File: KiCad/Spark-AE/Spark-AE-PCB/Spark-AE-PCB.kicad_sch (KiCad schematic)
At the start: 16 parts, among them J1 SSM-120-L-SV-BE, J2 SSM-120-L-SV-BE, J3 Conn_02x10_Odd_Even, J4 Conn_02x05_Odd_Even, J5 Conn_01x08_Socket, J6 Conn_01x08_Socket, J7 UJ32-C-V-G-TH-5-P24-TR, SW1 SW_Push, SW2 SW_Push, U1 PJS008U-3000-0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

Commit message: moving over progress from "Shock" (see desc)
I attempted to create this Daisy Pod clone as an AE-1U module called the "Shock". As expected I couldn't make it work.

I've moved my progress on the "Shock" schematic over to and replacing the work on the "Spark".

I plan to go back to make the "Shock" a stripped down version of the "Spark" in an AE-1U format.
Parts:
- removed J1, J2: SSM-120-L-SV-BE, clectric-diy:SAMTEC_SSM-120-L-SV-BE, symbol clectric-diy:SSM-120-L-SV-BE
- removed J3: Conn_02x10_Odd_Even, Connector_PinHeader_2.54mm:PinHeader_2x10_P2.54mm_Vertical, symbol Connector_Generic:Conn_02x10_Odd_Even
- removed J5, J6: Conn_01x08_Socket, Connector_PinSocket_2.54mm:PinSocket_1x08_P2.54mm_Vertical, symbol Connector:Conn_01x08_Socket
- removed J7: UJ32-C-V-G-TH-5-P24-TR, clectric-diy:SAMESKY_UJ32-C-V-G-TH-5-P24-TR, symbol clectric-diy:UJ32-C-V-G-TH-5-P24-TR
- removed LED1, LED2: WS2812B-V5/W, clectric-diy:LED-SMD_4P-L5.0-W5.0-TL-1, symbol clectric-diy:WS2812B-V5_W
- removed R1, R2: RK09K1130A8G, clectric-diy:RES-TH_RK09K113004U, symbol clectric-diy:RK09K1130A8G
- removed U1: PJS008U-3000-0, clectric-diy:PJS008U-3000-0, symbol clectric-diy:PJS008U-3000-0
- removed U2: Daisy_Seed, clectric-diy:DAISY_SEED, symbol clectric-diy:Daisy_Seed
- added C1, C2, C3: 10nF, Capacitor_SMD:C_0402_1005Metric, symbol Device:C
- added D1, D10, D11, D12, D13, D14, D15, D16, D17, D18, D2, D3, D4, D5, D6, D7, D8, D9: D, Diode_SMD:D_0402_1005Metric, symbol Device:D
- added J1, J2: Conn_01x09_Socket, Connector_PinSocket_2.54mm:PinSocket_1x09_P2.54mm_Vertical, symbol Connector:Conn_01x09_Socket
- added J3, J4: Conn_01x20_Pin, clectric-diy:Connector_PinSocket-1x20-P2.54mm_Mill-Max_315-13-120-41-004000, symbol Connector:Conn_01x20_Pin
- added J6: Conn_02x05_Odd_Even, Connector_PinHeader_2.54mm:PinHeader_2x05_P2.54mm_Vertical, symbol Connector_Generic:Conn_02x05_Odd_Even
- added LED1, LED2: A-SP1943B1GHR6C-C01-2T, clectric-diy:LED-SMD_4P-L1.6-W1.5-BL_A-SP1943B1GHR6C-C01-2T, symbol clectric-diy:LED-SMD_4P-L1.6-W1.5-BL_A-SP1943B1GHR6C-C01-2T
- added NT1: NetTie, NetTie:NetTie-3_SMD_Pad0.5mm, symbol Device:NetTie_3
- added POT1, POT2: RK09K1130D62, clectric-diy:RK09K1130D62, symbol clectric-diy:RK09K1130A8G
- added R1, R2, R4, R5: 150R, Resistor_SMD:R_0402_1005Metric, symbol clectric-diy:CR0603-FX-1001ELF
- added R10, R11, R12, R7, R8, R9: 10K, Resistor_SMD:R_0402_1005Metric, symbol Device:R
- added R3, R6: 330R, Resistor_SMD:R_0402_1005Metric, symbol clectric-diy:CR0603-FX-1001ELF
- added U1: WS2811, clectric-diy:SOP-8_L4.9-W3.9-P1.27-LS6.0-BL, symbol clectric-diy:WS2811
- added U3: Daisy_Seed, clectric-diy:DAISY_SEED, symbol clectric-diy:Daisy_Seed
- renumbered S1 to ENC1, J4 to J5
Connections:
- net +3V3_A: now also J3.1 (Pin_1), J6.1 (Pin_1), POT1.3, POT2.3, U3.21 (3V3_A)
- net +3V3_D: now also J3.18 (Pin_18), J6.2 (Pin_2), LED1.3, LED2.3, R10.2, R11.2, R9.2, U3.38 (3V3_D)
- net +5V: now also ENC1.5 (+_2), J3.19 (Pin_19), U1.8 (VDD), U3.39 (VIN)
- net A1_D16: now also D17.2 (A), D8.1 (K), J3.3 (Pin_3), U3.23 (D16)
- net A7_D22: now also D18.2 (A), D9.1 (K), J3.9 (Pin_9), U3.29 (D22)
- net AUDIO_IN_1: now also D1.1 (K), J4.16 (Pin_16), U3.16 (AUDIO_IN_1)
- net AUDIO_IN_2: now also D2.1 (K), J4.17 (Pin_17), U3.17 (AUDIO_IN_2)
- net AUDIO_OUT_1: now also D10.2 (A), J4.18 (Pin_18), U3.18 (AUDIO_OUT_1)
- net AUDIO_OUT_2: now also D11.2 (A), J4.19 (Pin_19), U3.19 (AUDIO_OUT_2)
- net ENC_A: now also J3.13 (Pin_13), R7.2, U3.33 (D26)
- net ENC_B: now also J3.12 (Pin_12), R8.2, U3.32 (D25)
- net ENC_CLICK: now also J4.14 (Pin_14), R12.2, U3.14 (D13)
- net GND: now also NT1.3
- net I2C_SCL: now also J4.12 (Pin_12), J6.5 (Pin_5), U3.12 (D11)
- net I2C_SDA: now also J4.13 (Pin_13), J6.6 (Pin_6), U3.13 (D12)
- net LED_1_B: now also J3.5 (Pin_5), LED1.2, R2.1, R2.2, U3.25 (D18)
- net LED_1_G: now also J3.6 (Pin_6), LED1.1, R1.1, R1.2, U3.26 (D19)
- net LED_1_R: now also J3.7 (Pin_7), LED1.4, R3.1, R3.2, U3.27 (D20)
- net LED_2_B: now also J3.10 (Pin_10), LED2.2, R5.1, R5.2, U3.30 (D23)
- net LED_2_G: now also J3.11 (Pin_11), LED2.1, R4.1, R4.2, U3.31 (D24)
- net LED_2_R: now also J3.4 (Pin_4), LED2.4, R6.1, R6.2, U3.24 (D17)
- net POT_1: now also J3.8 (Pin_8), POT1.2, U3.28 (D21)
- net POT_2: now also J3.2 (Pin_2), POT2.2, U3.22 (D15)
- net SD_CK: now also J4.7 (Pin_7), U3.7 (D6)
- net SD_CMD: now also J4.6 (Pin_6), U3.6 (D5)
- net SD_D0: now also J4.5 (Pin_5), U3.5 (D4)
- net SD_D1: now also J4.4 (Pin_4), U3.4 (D3)
- net SD_D2: now also J4.3 (Pin_3), U3.3 (D2)
- net SD_D3: now also J4.2 (Pin_2), U3.2 (D1)
- net SPI_MISO: now also J4.10 (Pin_10), J6.10 (Pin_10), U3.10 (D9)
- net SPI_MOSI: now also J4.11 (Pin_11), J6.8 (Pin_8), U1.6 (DIN), U3.11 (D10)
- net SPI_NSS: now also J4.8 (Pin_8), J6.7 (Pin_7), U3.8 (D7)
- net SPI_SCK: now also J4.9 (Pin_9), J6.9 (Pin_9), U3.9 (D8)
- net TAC_SWITCH_1: now also SW1.1, J3.14 (Pin_14), U3.34 (D27)
- net TAC_SWITCH_2: now also SW2.1, J3.15 (Pin_15), U3.35 (D28)
- net USB_OTG_FS_D+: now also J3.17 (Pin_17), U3.37 (D30)
- net USB_OTG_FS_D-: now also J3.16 (Pin_16), U3.36 (D29)
- net USB_OTG_FS_ID: now also J4.1 (Pin_1), U3.1 (D0)
- net AGND: now reaches SW2.2
- net AGND: now also SW1.2, J4.20 (Pin_20), J6.3 (Pin_3), NT1.2, POT1.1, POT1.4 (EH), POT1.5 (EH), POT2.1, POT2.4 (EH), POT2.5 (EH), U3.20 (AGND)
- net ENC_RED: now reaches ENC1.1 (-_1)
- net ENC_RED: now also U1.1 (OUTR)
- net ENC_GREEN: now reaches ENC1.2 (-_2)
- net ENC_GREEN: now also U1.2 (OUTG)
- net at ENC1.3 (COM): now also C3.1, R11.1, R12.1
- net ENC_BLUE: now reaches ENC1.4 (+_1)
- net ENC_BLUE: now also U1.3 (OUTB)
- net at ENC1.A1: now also C1.1, R7.1, R9.1
- net at ENC1.B1: now also C2.1, R10.1, R8.1
- net DGND: now reaches ENC1.C1
- net DGND: now also ENC1.MH1, ENC1.MH2, C1.2, C2.2, C3.2, J3.20 (Pin_20), J6.4 (Pin_4), NT1.1, U1.4 (GND), U3.40 (DGND)
- new net D14: D16.2 (A), D7.1 (K), J4.15 (Pin_15), U3.15 (D14)
- new net POT1_CV: D5.1 (K)
- new net POT2_CV: D6.1 (K)
- new net SW1_CV: D3.1 (K)
- new net SW2_CV: D4.1 (K)
- no-connect marks 0 -> 6
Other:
- title: Spark-AE-Upper -> Spark-AE-PCB
- moved on the sheet: ENC1, J5, SW1, SW2

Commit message: initial committ of completely reworked schematic. thanks gemini!
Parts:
- removed C1, C2, C3: 10nF, Capacitor_SMD:C_0402_1005Metric, symbol Device:C
- removed D1, D10, D11, D12, D13, D14, D15, D16, D17, D18, D2, D3, D4, D5, D6, D7, D8, D9: D, Diode_SMD:D_0402_1005Metric, symbol Device:D
- removed ENC1: PEL12T-4225S-S1024, clectric-diy:PEL12T4225SS1024, symbol clectric-diy:PEL12T-4225S-S1024
- removed J1, J2: Conn_01x09_Socket, Connector_PinSocket_2.54mm:PinSocket_1x09_P2.54mm_Vertical, symbol Connector:Conn_01x09_Socket
- removed J3, J4: Conn_01x20_Pin, clectric-diy:Connector_PinSocket-1x20-P2.54mm_Mill-Max_315-13-120-41-004000, symbol Connector:Conn_01x20_Pin
- removed J5, J6: Conn_02x05_Odd_Even, Connector_PinHeader_2.54mm:PinHeader_2x05_P2.54mm_Vertical, symbol Connector_Generic:Conn_02x05_Odd_Even
- removed LED1, LED2: A-SP1943B1GHR6C-C01-2T, clectric-diy:LED-SMD_4P-L1.6-W1.5-BL_A-SP1943B1GHR6C-C01-2T, symbol clectric-diy:LED-SMD_4P-L1.6-W1.5-BL_A-SP1943B1GHR6C-C01-2T
- removed NT1: NetTie, NetTie:NetTie-3_SMD_Pad0.5mm, symbol Device:NetTie_3
- removed POT1, POT2: RK09K1130D62, clectric-diy:RK09K1130D62, symbol clectric-diy:RK09K1130A8G
- removed R1, R2, R4, R5: 150R, Resistor_SMD:R_0402_1005Metric, symbol clectric-diy:CR0603-FX-1001ELF
- removed R10, R11, R12, R7, R8, R9: 10K, Resistor_SMD:R_0402_1005Metric, symbol Device:R
- removed R3, R6: 330R, Resistor_SMD:R_0402_1005Metric, symbol clectric-diy:CR0603-FX-1001ELF
- removed SW1, SW2: SW_Push, Button_Switch_THT:SW_PUSH_6mm, symbol Switch:SW_Push
- removed U1: WS2811, clectric-diy:SOP-8_L4.9-W3.9-P1.27-LS6.0-BL, symbol clectric-diy:WS2811
- removed U3: Daisy_Seed, clectric-diy:DAISY_SEED, symbol clectric-diy:Daisy_Seed
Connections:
- no-connect marks 6 -> 0
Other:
- added sheet Daisy Seed & Mount (Spark-AE-PCB-DaisySeed.kicad_sch)
- added sheet Digital Expansion (Spark-AE-PCB-Expansion.kicad_sch)
- added sheet Input & Output (1 of 2) (Spark-AE-PCB-IO-1of2.kicad_sch)
- added sheet Input & Output (2 of 2) (Spark-AE-PCB-IO-2of2.kicad_sch)
- added sheet Power & Regulation (Spark-AE-PCB-Power.kicad_sch)
- added sheet User Interface (Spark-AE-PCB-UI.kicad_sch)

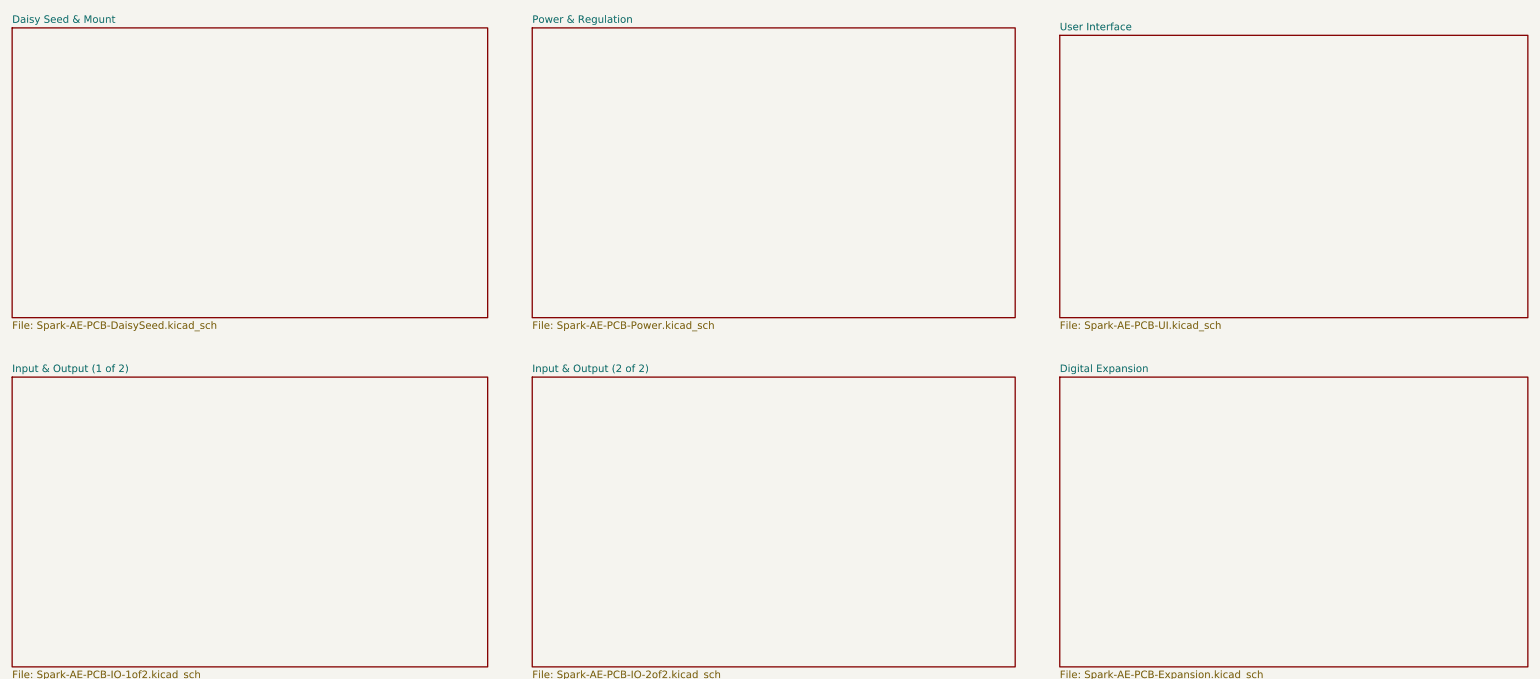
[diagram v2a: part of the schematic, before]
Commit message: schematic 100% complete. pcb layout around 50% complete.
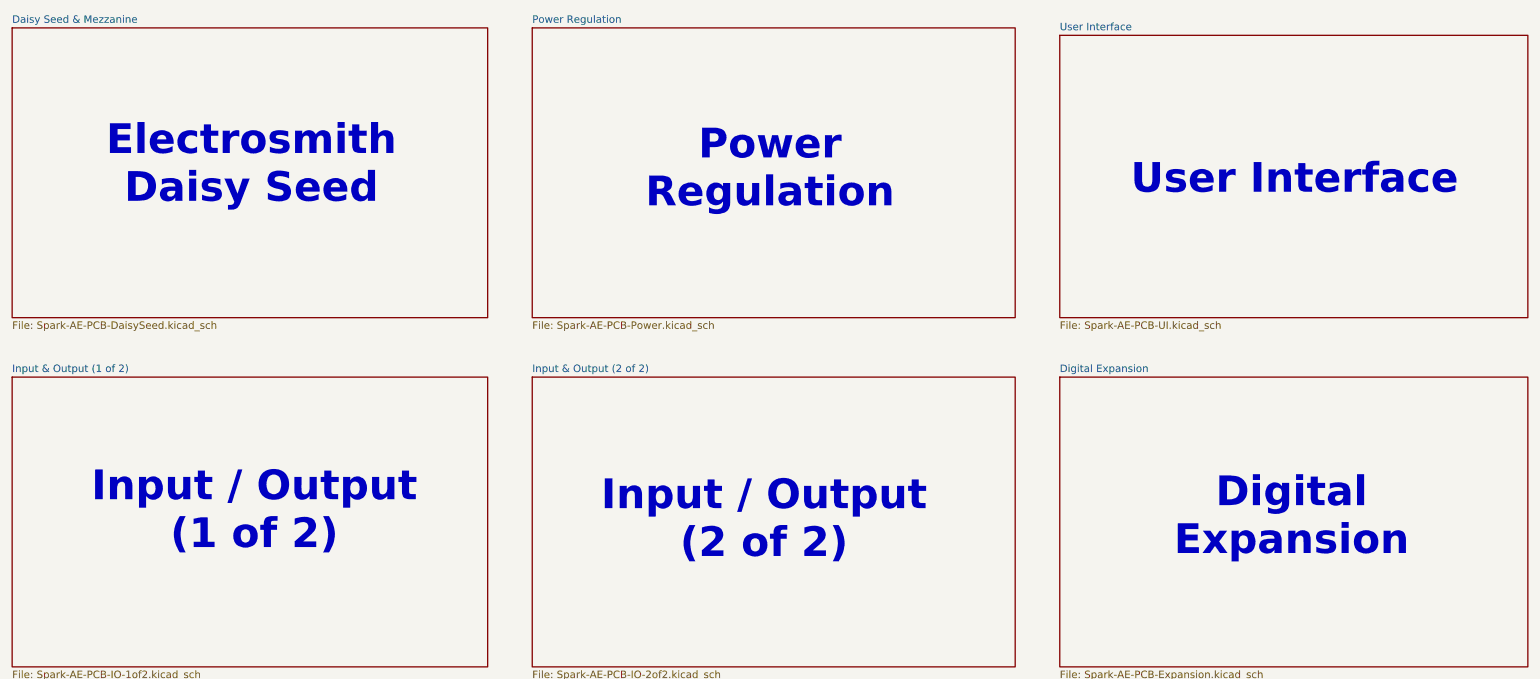
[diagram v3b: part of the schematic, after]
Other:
- sheet Daisy Seed & Mount renamed Daisy Seed & Mezzanine
- sheet Power & Regulation renamed Power Regulation
- note added: "Digital Expansion"
- note added: "Electrosmith Daisy Seed"
- note added: "Input / Output (1 of 2)"
- note added: "Input / Output (2 of 2)"
- note added: "Power Regulation"
- note added: "User Interface"
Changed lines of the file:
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@@
 		(comment 1 "Charles H. Leggett")
+	)
+	(text "Input / Output\n(2 of 2)"
+		(exclude_from_sim no)
+		(at 148.844 119.634 0)
+		(effects
+			(font
+				(size 5.08 5.08)
+				(thickness 1.016)
+				(bold yes)
+			)
+		)
+	)
+	(text "Digital\nExpansion"
+		(exclude_from_sim no)
+		(at 239.014 119.126 0)
+		(effects
+			(font
+				(size 5.08 5.08)
+				(thickness 1.016)
+				(bold yes)
+			)
+		)
+	)
+	(text "User Interface"
+		(exclude_from_sim no)
+		(at 239.522 61.468 0)
+		(effects
+			(font
+				(size 5.08 5.08)
+				(thickness 1.016)
+				(bold yes)
+			)
+		)
+	)
+	(text "Input / Output\n(1 of 2)"
+		(exclude_from_sim no)
+		(at 61.722 118.11 0)
+		(effects
+			(font
+				(size 5.08 5.08)
+				(thickness 1.016)
+				(bold yes)
+			)
+		)
+	)
+	(text "Power\nRegulation\n"
+		(exclude_from_sim no)
+		(at 149.86 59.69 0)
+		(effects
+			(font
+				(size 5.08 5.08)
+				(thickness 1.016)
+				(bold yes)
+			)
+		)
+	)
+	(text "Electrosmith\nDaisy Seed"
+		(exclude_from_sim no)
+		(at 61.214 58.928 0)
+		(effects
+			(font
+				(size 5.08 5.08)
+				(thickness 1.016)
+				(bold yes)
+			)
+		)
 	)
 	(sheet
@@
 			(color 0 0 0 0.0000)
 		)
-		(property "Sheetname" "Power & Regulation"
+		(property "Sheetname" "Power Regulation"
 			(at 109.22 34.8484 0)
 			(effects
@@
 			(color 0 0 0 0.0000)
 		)
-		(property "Sheetname" "Daisy Seed & Mount"
+		(property "Sheetname" "Daisy Seed & Mezzanine"
 			(at 20.32 34.8484 0)
 			(effects
